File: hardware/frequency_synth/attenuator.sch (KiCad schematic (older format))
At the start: 33 parts

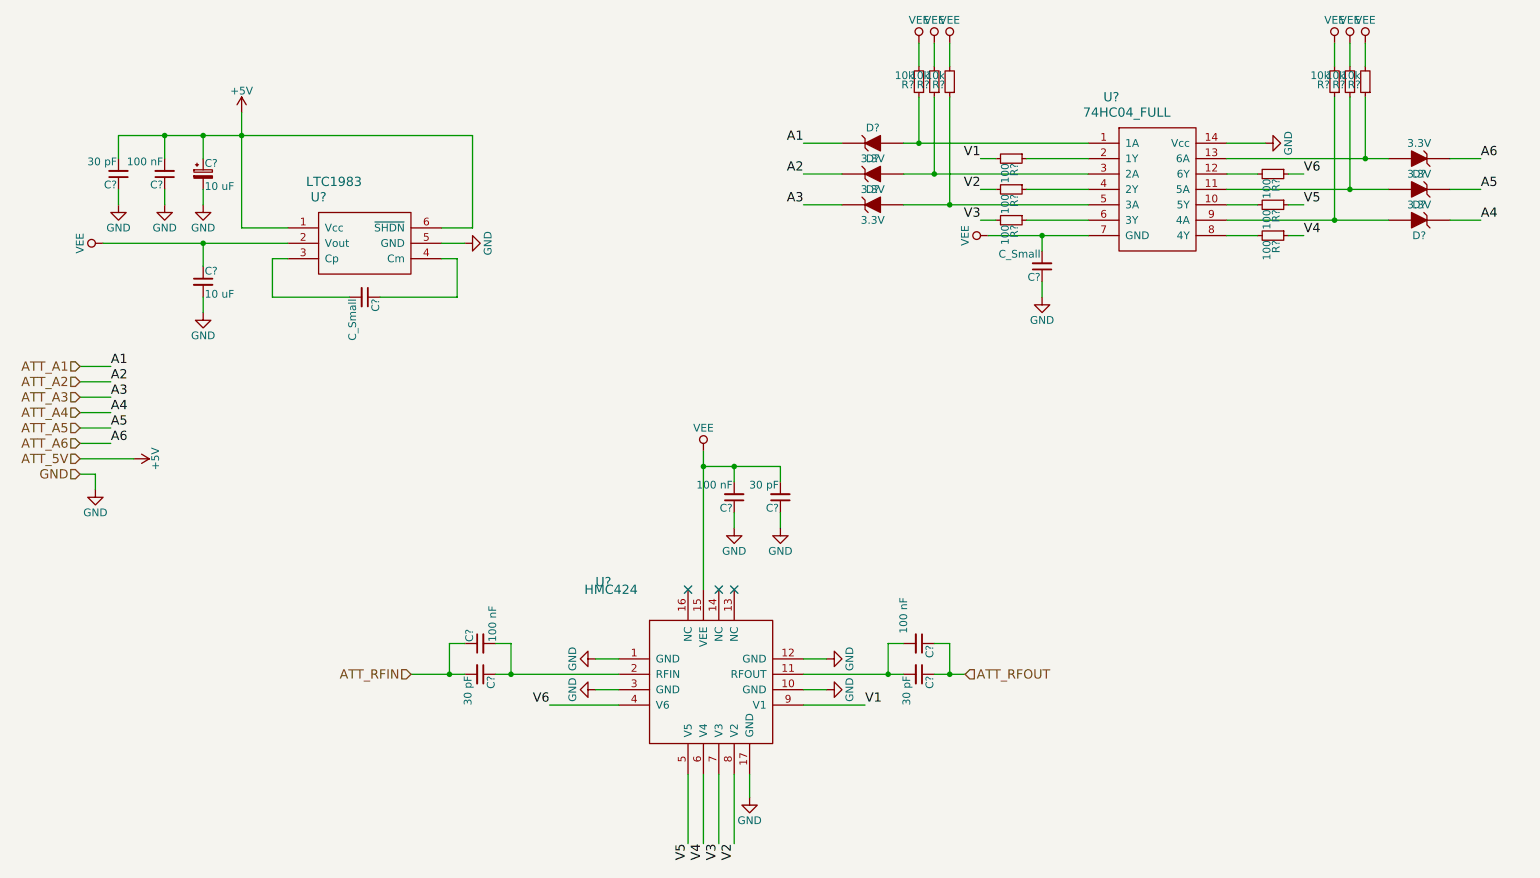
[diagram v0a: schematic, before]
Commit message: finished initial schematic of synth module
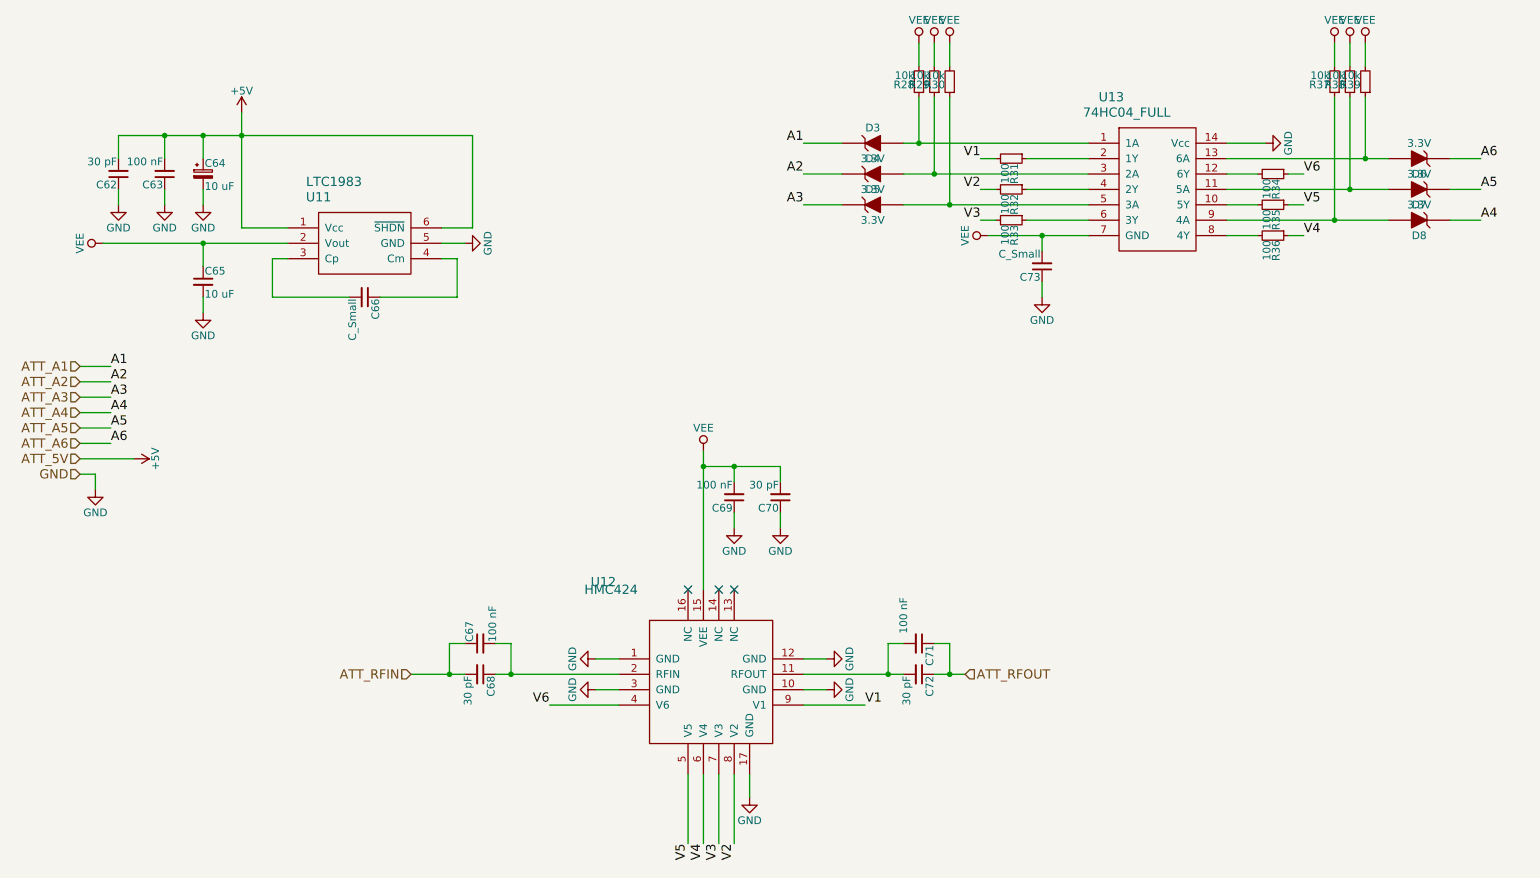
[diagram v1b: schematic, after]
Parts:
- gave numbers to parts that had none: 33

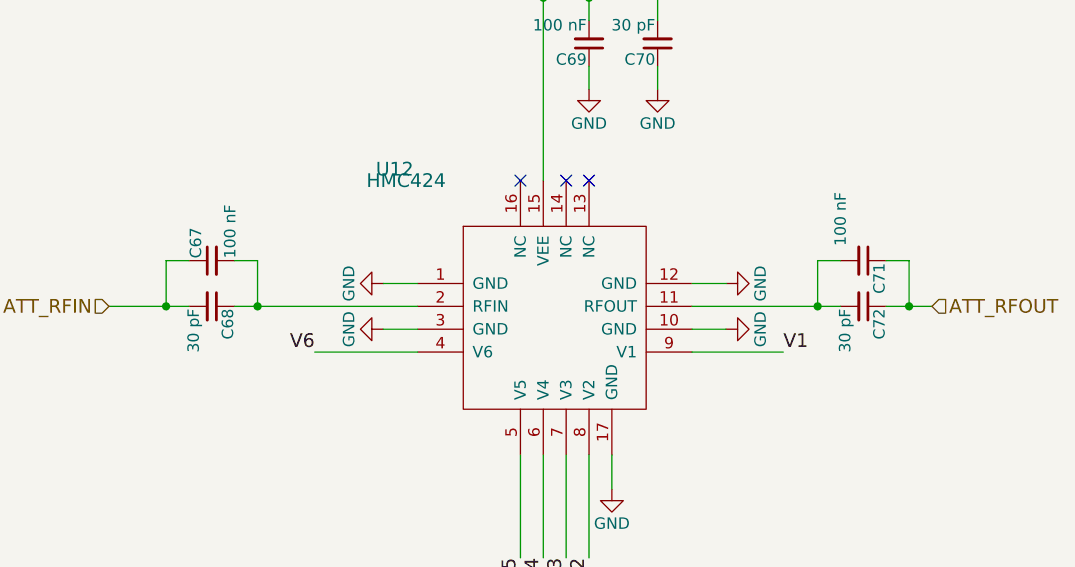
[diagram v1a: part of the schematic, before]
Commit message: reducing component values across module, synth schematic cleanups
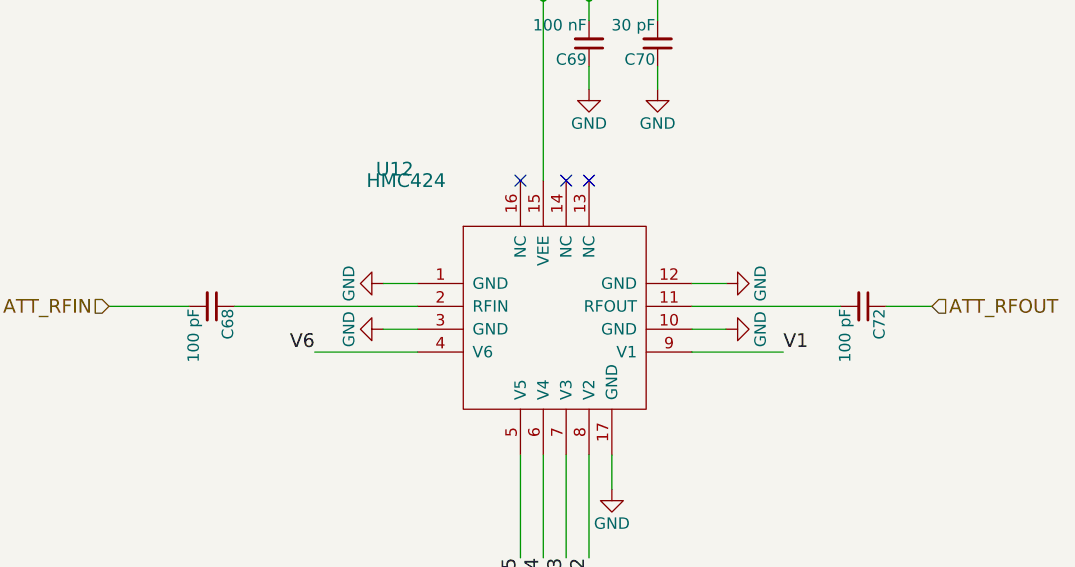
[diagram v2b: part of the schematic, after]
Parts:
- removed C67, C71: 100 nF, Capacitors_SMD:C_0402, symbol C_Small
- C64, C65, C66: footprint Capacitors_SMD:C_0805 -> Capacitors_SMD:C_0603
- C68, C72: value 30 pF -> 100 pF
- U13: footprint (none) -> Housings_SSOP:TSSOP-14_4.4x5mm_Pitch0.65mm
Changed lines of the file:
@@
 LIBS:74hc04
 LIBS:74hc04_full
+LIBS:conn_sma_2gnd
 LIBS:frequency_synth-cache
-LIBS:boosterpack-cache
-LIBS:refclk_breakout-cache
 EELAYER 25 0
 EELAYER END
@@
 P 3700 5250
 F 0 "C68" H 3710 5320 50  0000 L CNN
-F 1 "30 pF" H 3710 5170 50  0000 L CNN
+F 1 "100 pF" H 3710 5170 50  0000 L CNN
 F 2 "Capacitors_SMD:C_0402" H 3700 5250 50  0001 C CNN
 F 3 "" H 3700 5250 50  0000 C CNN
@@
 P 6550 5250
 F 0 "C72" H 6560 5320 50  0000 L CNN
-F 1 "30 pF" H 6560 5170 50  0000 L CNN
+F 1 "100 pF" H 6560 5170 50  0000 L CNN
 F 2 "Capacitors_SMD:C_0402" H 6550 5250 50  0001 C CNN
 F 3 "" H 6550 5250 50  0000 C CNN
@@
 $EndComp
 $Comp
-L GND #PWR136
+L GND #PWR151
 U 1 1 572AE6C7
 P 8800 1800
-F 0 "#PWR136" H 8800 1550 50  0001 C CNN
+F 0 "#PWR151" H 8800 1550 50  0001 C CNN
 F 1 "GND" H 8800 1650 50  0000 C CNN
 F 2 "" H 8800 1800 50  0000 C CNN
@@
 	8800 1800 8550 1800
 $Comp
-L VEE #PWR134
+L VEE #PWR149
 U 1 1 572AE6C8
 P 7000 2400
-F 0 "#PWR134" H 7000 2250 50  0001 C CNN
+F 0 "#PWR149" H 7000 2250 50  0001 C CNN
 F 1 "VEE" H 7000 2550 50  0000 C CNN
 F 2 "" H 7000 2400 50  0000 C CNN
@@
 $EndComp
 $Comp
-L GND #PWR135
+L GND #PWR150
 U 1 1 572AE6CA
 P 7350 2800
-F 0 "#PWR135" H 7350 2550 50  0001 C CNN
+F 0 "#PWR150" H 7350 2550 50  0001 C CNN
 F 1 "GND" H 7350 2650 50  0000 C CNN
 F 2 "" H 7350 2800 50  0000 C CNN
@@
 	9450 1300 9450 1150
 $Comp
-L VEE #PWR131
+L VEE #PWR146
 U 1 1 572AE6D7
 P 6550 1150
-F 0 "#PWR131" H 6550 1000 50  0001 C CNN
+F 0 "#PWR146" H 6550 1000 50  0001 C CNN
 F 1 "VEE" H 6550 1300 50  0000 C CNN
 F 2 "" H 6550 1150 50  0000 C CNN
@@
 $EndComp
 $Comp
-L VEE #PWR132
+L VEE #PWR147
 U 1 1 572AE6D8
 P 6650 1150
-F 0 "#PWR132" H 6650 1000 50  0001 C CNN
+F 0 "#PWR147" H 6650 1000 50  0001 C CNN
 F 1 "VEE" H 6650 1300 50  0000 C CNN
 F 2 "" H 6650 1150 50  0000 C CNN
@@
 $EndComp
 $Comp
-L VEE #PWR133
+L VEE #PWR148
 U 1 1 572AE6D9
 P 6750 1150
-F 0 "#PWR133" H 6750 1000 50  0001 C CNN
+F 0 "#PWR148" H 6750 1000 50  0001 C CNN
 F 1 "VEE" H 6750 1300 50  0000 C CNN
 F 2 "" H 6750 1150 50  0000 C CNN
@@
 $EndComp
 $Comp
-L VEE #PWR137
+L VEE #PWR152
 U 1 1 572AE6DA
 P 9250 1150
-F 0 "#PWR137" H 9250 1000 50  0001 C CNN
+F 0 "#PWR152" H 9250 1000 50  0001 C CNN
 F 1 "VEE" H 9250 1300 50  0000 C CNN
 F 2 "" H 9250 1150 50  0000 C CNN
@@
 $EndComp
 $Comp
-L VEE #PWR138
+L VEE #PWR153
 U 1 1 572AE6DB
 P 9350 1150
-F 0 "#PWR138" H 9350 1000 50  0001 C CNN
+F 0 "#PWR153" H 9350 1000 50  0001 C CNN
 F 1 "VEE" H 9350 1300 50  0000 C CNN
 F 2 "" H 9350 1150 50  0000 C CNN
@@
 $EndComp
 $Comp
-L VEE #PWR139
+L VEE #PWR154
 U 1 1 572AE6DC
 P 9450 1150
-F 0 "#PWR139" H 9450 1000 50  0001 C CNN
+F 0 "#PWR154" H 9450 1000 50  0001 C CNN
 F 1 "VEE" H 9450 1300 50  0000 C CNN
 F 2 "" H 9450 1150 50  0000 C CNN
@@
 	6650 5250 6850 5250
 Wire Wire Line
-	3250 5250 3600 5250
-Wire Wire Line
 	5800 5250 6450 5250
 $Comp
-L GND #PWR129
+L GND #PWR144
 U 1 1 572AE6DF
 P 5950 5150
-F 0 "#PWR129" H 5950 4900 50  0001 C CNN
+F 0 "#PWR144" H 5950 4900 50  0001 C CNN
 F 1 "GND" H 5950 5000 50  0000 C CNN
 F 2 "" H 5950 5150 50  0000 C CNN
@@
 	5950 5150 5800 5150
 $Comp
-L GND #PWR130
+L GND #PWR145
 U 1 1 572AE6E0
 P 5950 5350
-F 0 "#PWR130" H 5950 5100 50  0001 C CNN
+F 0 "#PWR145" H 5950 5100 50  0001 C CNN
 F 1 "GND" H 5950 5200 50  0000 C CNN
 F 2 "" H 5950 5350 50  0000 C CNN
@@
 	5950 5350 5800 5350
 $Comp
-L GND #PWR127
+L GND #PWR142
 U 1 1 572AE6E1
 P 5450 6050
-F 0 "#PWR127" H 5450 5800 50  0001 C CNN
+F 0 "#PWR142" H 5450 5800 50  0001 C CNN
 F 1 "GND" H 5450 5900 50  0000 C CNN
 F 2 "" H 5450 6050 50  0000 C CNN
@@
 	5450 6050 5450 5900
 $Comp
-L GND #PWR124
+L GND #PWR139
 U 1 1 572AE6E2
 P 4450 5350
-F 0 "#PWR124" H 4450 5100 50  0001 C CNN
+F 0 "#PWR139" H 4450 5100 50  0001 C CNN
 F 1 "GND" H 4450 5200 50  0000 C CNN
 F 2 "" H 4450 5350 50  0000 C CNN
@@
 $EndComp
 $Comp
-L GND #PWR123
+L GND #PWR138
 U 1 1 572AE6E3
 P 4450 5150
-F 0 "#PWR123" H 4450 4900 50  0001 C CNN
+F 0 "#PWR138" H 4450 4900 50  0001 C CNN
 F 1 "GND" H 4450 5000 50  0000 C CNN
 F 2 "" H 4450 5150 50  0000 C CNN
@@
 	4450 5350 4600 5350
 $Comp
-L VEE #PWR125
+L VEE #PWR140
 U 1 1 572AE6E4
 P 5150 3800
-F 0 "#PWR125" H 5150 3650 50  0001 C CNN
+F 0 "#PWR140" H 5150 3650 50  0001 C CNN
 F 1 "VEE" H 5150 3950 50  0000 C CNN
 F 2 "" H 5150 3800 50  0000 C CNN
@@
 $EndComp
 $Comp
-L GND #PWR126
+L GND #PWR141
 U 1 1 572AE6E6
 P 5350 4300
-F 0 "#PWR126" H 5350 4050 50  0001 C CNN
+F 0 "#PWR141" H 5350 4050 50  0001 C CNN
 F 1 "GND" H 5350 4150 50  0000 C CNN
 F 2 "" H 5350 4300 50  0000 C CNN
@@
 	5050 5900 5050 6350
 $Comp
-L GND #PWR114
+L GND #PWR129
 U 1 1 572AE6E8
 P 1200 4050
-F 0 "#PWR114" H 1200 3800 50  0001 C CNN
+F 0 "#PWR129" H 1200 3800 50  0001 C CNN
 F 1 "GND" H 1200 3900 50  0000 C CNN
 F 2 "" H 1200 4050 50  0000 C CNN
@@
 $EndComp
 $Comp
-L +5V #PWR117
+L +5V #PWR132
 U 1 1 572AE6EA
 P 1450 3850
-F 0 "#PWR117" H 1450 3700 50  0001 C CNN
+F 0 "#PWR132" H 1450 3700 50  0001 C CNN
 F 1 "+5V" H 1450 3990 50  0000 C CNN
 F 2 "" H 1450 3850 50  0000 C CNN
@@
 	1450 3850 1100 3850
 $Comp
-L VEE #PWR115
+L VEE #PWR130
 U 1 1 572AE6EB
 P 1250 2450
-F 0 "#PWR115" H 1250 2300 50  0001 C CNN
+F 0 "#PWR130" H 1250 2300 50  0001 C CNN
 F 1 "VEE" H 1250 2600 50  0000 C CNN
 F 2 "" H 1250 2450 50  0000 C CNN
@@
 $EndComp
 $Comp
-L +5V #PWR121
+L +5V #PWR136
 U 1 1 572AE6EC
 P 2150 1600
-F 0 "#PWR121" H 2150 1450 50  0001 C CNN
+F 0 "#PWR136" H 2150 1450 50  0001 C CNN
 F 1 "+5V" H 2150 1740 50  0000 C CNN
 F 2 "" H 2150 1600 50  0000 C CNN
@@
 F 0 "C66" H 2960 2870 50  0000 L CNN
 F 1 "C_Small" H 2960 2720 50  0000 L CNN
-F 2 "Capacitors_SMD:C_0805" H 2950 2800 50  0001 C CNN
+F 2 "Capacitors_SMD:C_0603" H 2950 2800 50  0001 C CNN
 F 3 "" H 2950 2800 50  0000 C CNN
 	1    2950 2800
@@
 	3550 2550 3450 2550
 $Comp
-L GND #PWR122
+L GND #PWR137
 U 1 1 572AE6EE
 P 3600 2450
-F 0 "#PWR122" H 3600 2200 50  0001 C CNN
+F 0 "#PWR137" H 3600 2200 50  0001 C CNN
 F 1 "GND" H 3600 2300 50  0000 C CNN
 F 2 "" H 3600 2450 50  0000 C CNN
@@
 F 0 "C65" H 1910 2770 50  0000 L CNN
 F 1 "10 uF" H 1910 2620 50  0000 L CNN
-F 2 "Capacitors_SMD:C_0805" H 1900 2700 50  0001 C CNN
+F 2 "Capacitors_SMD:C_0603" H 1900 2700 50  0001 C CNN
 F 3 "" H 1900 2700 50  0000 C CNN
 	1    1900 2700
@@
 $EndComp
 $Comp
-L GND #PWR120
+L GND #PWR135
 U 1 1 572AE6F0
 P 1900 2900
-F 0 "#PWR120" H 1900 2650 50  0001 C CNN
+F 0 "#PWR135" H 1900 2650 50  0001 C CNN
 F 1 "GND" H 1900 2750 50  0000 C CNN
 F 2 "" H 1900 2900 50  0000 C CNN
@@
 Connection ~ 1900 2450
 $Comp
-L GND #PWR119
+L GND #PWR134
 U 1 1 572AE6F1
 P 1900 2200
-F 0 "#PWR119" H 1900 1950 50  0001 C CNN
+F 0 "#PWR134" H 1900 1950 50  0001 C CNN
 F 1 "GND" H 1900 2050 50  0000 C CNN
 F 2 "" H 1900 2200 50  0000 C CNN
@@
 F 0 "C64" H 1910 2070 50  0000 L CNN
 F 1 "10 uF" H 1910 1920 50  0000 L CNN
-F 2 "Capacitors_SMD:C_0805" H 1900 2000 50  0001 C CNN
+F 2 "Capacitors_SMD:C_0603" H 1900 2000 50  0001 C CNN
 F 3 "" H 1900 2000 50  0000 C CNN
 	1    1900 2000
@@
 $EndComp
 $Comp
-L GND #PWR118
+L GND #PWR133
 U 1 1 572AE6F4
 P 1650 2200
-F 0 "#PWR118" H 1650 1950 50  0001 C CNN
+F 0 "#PWR133" H 1650 1950 50  0001 C CNN
 F 1 "GND" H 1650 2050 50  0000 C CNN
 F 2 "" H 1650 2200 50  0000 C CNN
@@
 $EndComp
 $Comp
-L GND #PWR128
+L GND #PWR143
 U 1 1 572AE6F6
 P 5650 4300
-F 0 "#PWR128" H 5650 4050 50  0001 C CNN
+F 0 "#PWR143" H 5650 4050 50  0001 C CNN
 F 1 "GND" H 5650 4150 50  0000 C CNN
 F 2 "" H 5650 4300 50  0000 C CNN
@@
 $EndComp
 $Comp
-L GND #PWR116
+L GND #PWR131
 U 1 1 572AE6F8
 P 1350 2200
-F 0 "#PWR116" H 1350 1950 50  0001 C CNN
+F 0 "#PWR131" H 1350 1950 50  0001 C CNN
 F 1 "GND" H 1350 2050 50  0000 C CNN
 F 2 "" H 1350 2200 50  0000 C CNN
@@
 	1350 1900 1350 1750
 Connection ~ 1650 1750
-$Comp
-L C_Small C67
-U 1 1 572AE6F9
-P 3700 5050
-F 0 "C67" H 3710 5120 50  0000 L CNN
-F 1 "100 nF" H 3710 4970 50  0000 L CNN
-F 2 "Capacitors_SMD:C_0402" H 3700 5050 50  0001 C CNN
-F 3 "" H 3700 5050 50  0000 C CNN
-	1    3700 5050
-	0    -1   -1   0
-$EndComp
-Wire Wire Line
-	3600 5050 3500 5050
-Wire Wire Line
-	3500 5050 3500 5250
-Connection ~ 3500 5250
-Wire Wire Line
-	3800 5050 3900 5050
-Wire Wire Line
-	3900 5050 3900 5250
-Connection ~ 3900 5250
-$Comp
-L C_Small C71
-U 1 1 572AE6FA
-P 6550 5050
-F 0 "C71" H 6560 5120 50  0000 L CNN
-F 1 "100 nF" H 6250 4950 50  0000 L CNN
-F 2 "Capacitors_SMD:C_0402" H 6550 5050 50  0001 C CNN
-F 3 "" H 6550 5050 50  0000 C CNN
-	1    6550 5050
-	0    1    1    0
-$EndComp
-Wire Wire Line
-	6450 5050 6350 5050
-Wire Wire Line
-	6350 5050 6350 5250
-Connection ~ 6350 5250
-Wire Wire Line
-	6650 5050 6750 5050
-Wire Wire Line
-	6750 5050 6750 5250
-Connection ~ 6750 5250
 Text HLabel 1100 3250 0    60   Input ~ 0
 ATT_A1
@@
 F 0 "U13" H 7800 2700 60  0000 C CNN
 F 1 "74HC04_FULL" H 7900 2600 60  0000 C CNN
-F 2 "" H 8100 2100 60  0000 C CNN
+F 2 "Housings_SSOP:TSSOP-14_4.4x5mm_Pitch0.65mm" H 8100 2100 60  0001 C CNN
 F 3 "" H 8100 2100 60  0000 C CNN
 	1    8100 2100
 	1    0    0    -1
 $EndComp
+Wire Wire Line
+	3250 5250 3600 5250
 $EndSCHEMATC
